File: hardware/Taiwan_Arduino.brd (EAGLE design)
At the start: 97.4 x 35.6 mm, 43 parts, among them J1 AVR_SPI_PRG_62X3_LOCK, T2 2N2222, U1 ATMEGA328P_PDIP, U2 SPI_FLASH, Y2 16mhz

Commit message: add FTDI pin labels
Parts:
- FTDI: value DTR -> (none)
- moved S1 2.04 mm to (18.1, 17.4)
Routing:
- net +5V: track 159.4 -> 144.5 mm
- net RST: track 53.4 -> 47.5 mm
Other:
- board text added: "DTR RXI TXO VCC CTS GND"
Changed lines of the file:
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@@
 <?xml version="1.0" encoding="utf-8"?>
 <!DOCTYPE eagle SYSTEM "eagle.dtd">
-<eagle version="7.4.0">
+<eagle version="7.2.0">
 <drawing>
 <settings>
@@
 <text x="57.3" y="12.1" size="1.016" layer="21" font="vector" ratio="15">22pf</text>
 <text x="47.7" y="37.9" size="1.016" layer="21" font="vector" ratio="15" rot="R180">104</text>
-<text x="21.2" y="20" size="1.016" layer="21" font="vector" ratio="15" rot="R180">Reset</text>
+<text x="25.7" y="21.4" size="1.016" layer="21" font="vector" ratio="15" rot="R180">Reset</text>
 <text x="22.9" y="14.5" size="1.016" layer="21" font="vector" ratio="15">104</text>
 <text x="78.5" y="9.8" size="1.4224" layer="21" font="vector" ratio="15" rot="R180">D6</text>
@@
 <text x="14.7" y="21.4" size="1.4224" layer="21" font="vector" ratio="15">A5</text>
 <text x="66.8" y="8.6" size="1.4224" layer="21" font="vector" ratio="15">D7</text>
+<text x="13.5" y="12" size="0.8128" layer="22" font="vector" ratio="15" distance="60" rot="MR90">DTR
+RXI
+TXO
+VCC
+CTS
+GND</text>
 </plain>
 <attributes>
@@
 <element name="TP8" library="SparkFun-Passives" package="PADBIG" value="TEST-POINT" x="90.575859375" y="17.7033125" rot="R200"/>
 <element name="TP9" library="SparkFun-Passives" package="PADBIG" value="TEST-POINT" x="80.3756375" y="27.159590625" rot="R200"/>
-<element name="FTDI" library="SparkFun-Connectors" package="1X06_LOCK" value="DTR" x="26.8" y="10.4" smashed="yes" rot="R180">
-<attribute name="NAME" x="28.378" y="9.97" size="1.016" layer="25" font="vector" ratio="15" rot="R270"/>
-<attribute name="VALUE" x="27.97" y="9.102" size="1.016" layer="27" font="vector" ratio="15" rot="R180"/>
+<element name="FTDI" library="SparkFun-Connectors" package="1X06_LOCK" value="" x="26.8" y="10.4" smashed="yes" rot="R180">
+<attribute name="NAME" x="26.23" y="7.578" size="1.016" layer="25" font="vector" ratio="15"/>
+<attribute name="VALUE" x="26.77" y="8.902" size="1.016" layer="27" font="vector" ratio="15" rot="R180"/>
 </element>
 <element name="RV1" library="SparkFun-Electromechanical" package="ALPS_POT" value="5k" x="69.229653125" y="20.472284375" smashed="yes" rot="R90">
@@
 <attribute name="NAME" x="50.25269375" y="34.93434375" size="1.016" layer="25" font="vector" ratio="15" rot="R270"/>
 </element>
-<element name="S1" library="SparkFun-Electromechanical" package="TACTILE-PTH" value="SWITCH-MOMENTARY-2PTH" x="17.66" y="15.35" smashed="yes" rot="R180">
-<attribute name="NAME" x="16.016521875" y="20.03429375" size="1.016" layer="25" font="vector" ratio="15" rot="R180"/>
+<element name="S1" library="SparkFun-Electromechanical" package="TACTILE-PTH" value="SWITCH-MOMENTARY-2PTH" x="18.06" y="17.35" smashed="yes" rot="R180">
+<attribute name="NAME" x="14.53429375" y="16.583478125" size="1.016" layer="25" font="vector" ratio="15" rot="R90"/>
 </element>
 <element name="D1" library="SparkFun-LED" package="LED3MM" value="" x="41.3" y="28.6" smashed="yes" rot="R180">
@@
 <wire x1="44.469140625" y1="14.361278125" x2="44.469140625" y2="16.652325" width="0.6096" layer="1"/>
 <wire x1="44.469140625" y1="16.652325" x2="44.048196875" y2="17.17326875" width="0.6096" layer="1"/>
-<wire x1="26" y1="19.44" x2="20.14" y2="19.44" width="0.254" layer="1"/>
-<wire x1="20.14" y1="19.44" x2="19.3" y2="18.6" width="0.254" layer="1"/>
-<wire x1="19.3" y1="18.6" x2="19.3" y2="10.774" width="0.254" layer="1"/>
+<wire x1="26" y1="19.44" x2="21.64" y2="18.44" width="0" layer="19" extent="1-16"/>
+<wire x1="21.64" y1="18.44" x2="19.3" y2="18.6" width="0" layer="19" extent="1-16"/>
+<wire x1="19.3" y1="18.6" x2="19.3" y2="10.774" width="0" layer="19" extent="1-16"/>
 <wire x1="19.3" y1="10.774" x2="19.18" y2="10.654" width="0.254" layer="1"/>
 <wire x1="44.9" y1="36.8" x2="44.2" y2="36" width="1.016" layer="1"/>
@@
 <wire x1="55.2" y1="21.9" x2="56.1" y2="22.8" width="0.254" layer="16"/>
 <via x="56.1" y="22.8" extent="1-16" drill="0.3302"/>
-<wire x1="28.434928125" y1="16.3" x2="28.5" y2="16.2" width="0.254" layer="1"/>
-<wire x1="28.5" y1="16.2" x2="28.6" y2="16.9" width="0.254" layer="1"/>
 <wire x1="28.6" y1="16.9" x2="28.6" y2="20.7" width="0.254" layer="1"/>
 <wire x1="28.6" y1="20.7" x2="29.3" y2="21.4" width="0.254" layer="1"/>
-<wire x1="26" y1="16.9" x2="28.734928125" y2="16.9" width="0.254" layer="1"/>
-<wire x1="28.734928125" y1="16.9" x2="28.808196875" y2="17.17326875" width="0.254" layer="1"/>
 <wire x1="56.1" y1="22.8" x2="57.7" y2="22.8" width="0.254" layer="1"/>
 <wire x1="57.7" y1="22.8" x2="57.9" y2="23" width="0.254" layer="1"/>
 <wire x1="57.9" y1="23" x2="57.9" y2="27.757859375" width="0.254" layer="1"/>
 <wire x1="57.9" y1="27.757859375" x2="57.3817875" y2="28.276071875" width="0.254" layer="1"/>
-<wire x1="26" y1="16.9" x2="22.0218" y2="16.9" width="0.254" layer="1"/>
-<wire x1="22.0218" y1="16.9" x2="20.9112" y2="17.6106" width="0.254" layer="1"/>
 <wire x1="23.2" y1="13.4" x2="23.2" y2="14.1" width="0.254" layer="1"/>
 <wire x1="23.2" y1="14.1" x2="26" y2="16.9" width="0.254" layer="1"/>
-<wire x1="28.734928125" y1="16.9" x2="28.6" y2="16.9" width="0" layer="19" extent="1-1"/>
+<wire x1="28.734928125" y1="16.9" x2="28.808196875" y2="16.97326875" width="0.254" layer="1"/>
+<wire x1="28.808196875" y1="16.97326875" x2="28.808196875" y2="17.17326875" width="0.254" layer="1"/>
+<wire x1="26" y1="16.9" x2="28.534928125" y2="16.9" width="0.254" layer="1"/>
+<wire x1="28.534928125" y1="16.9" x2="28.808196875" y2="17.17326875" width="0.254" layer="1"/>
+<wire x1="28.534928125" y1="16.9" x2="28.6" y2="16.9" width="0" layer="19" extent="1-1"/>
+<wire x1="21.3112" y1="19.6106" x2="23.2" y2="13.4" width="0" layer="19" extent="1-1"/>
 </signal>
 <signal name="N$10">

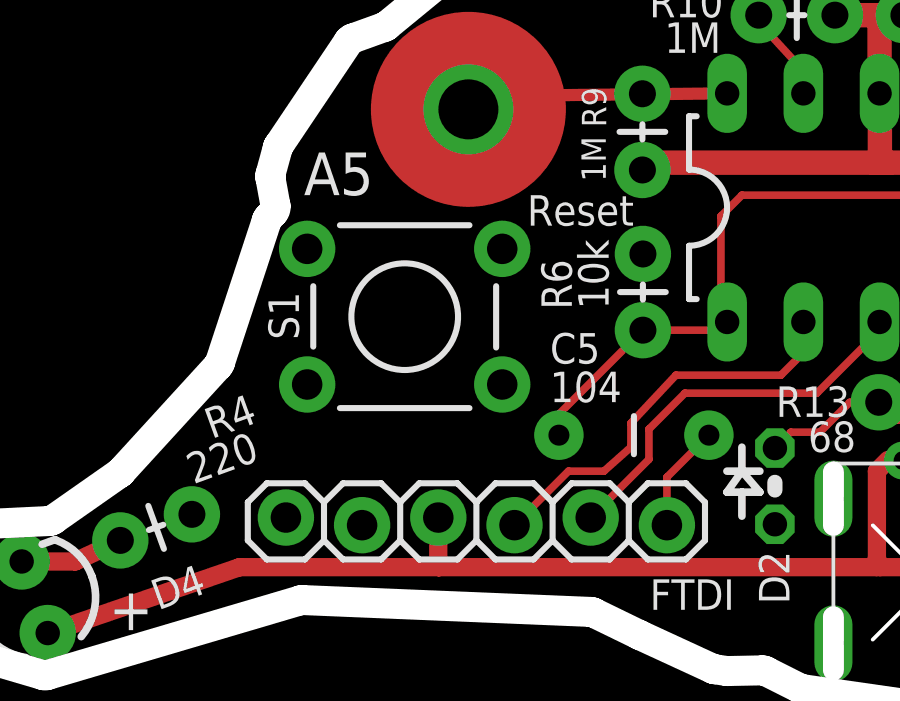
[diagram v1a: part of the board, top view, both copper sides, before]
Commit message: add FTDI Tag
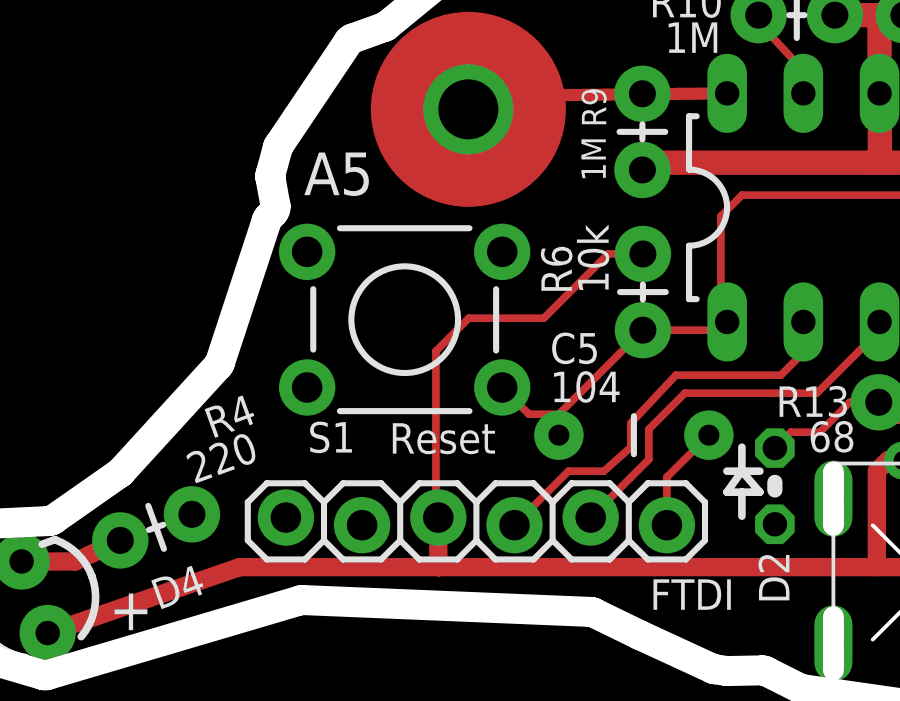
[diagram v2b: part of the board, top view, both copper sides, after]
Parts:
- moved S1 0.10 mm to (18.1, 17.2)
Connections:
- net GND: now also S1.3; no longer S1.1
- net RST: now also S1.1; no longer S1.3
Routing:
- net +5V: track 144.5 -> 158.4 mm
- net RST: track 47.5 -> 49.7 mm
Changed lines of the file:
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@@
 <?xml version="1.0" encoding="utf-8"?>
 <!DOCTYPE eagle SYSTEM "eagle.dtd">
-<eagle version="7.2.0">
+<eagle version="7.4.0">
 <drawing>
 <settings>
@@
 <text x="57.3" y="12.1" size="1.016" layer="21" font="vector" ratio="15">22pf</text>
 <text x="47.7" y="37.9" size="1.016" layer="21" font="vector" ratio="15" rot="R180">104</text>
-<text x="25.7" y="21.4" size="1.016" layer="21" font="vector" ratio="15" rot="R180">Reset</text>
+<text x="21.1" y="13.8" size="1.016" layer="21" font="vector" ratio="15" rot="R180">Reset</text>
 <text x="22.9" y="14.5" size="1.016" layer="21" font="vector" ratio="15">104</text>
 <text x="78.5" y="9.8" size="1.4224" layer="21" font="vector" ratio="15" rot="R180">D6</text>
@@
 </element>
 <element name="R6" library="SparkFun-Resistors" package="AXIAL-0.1" value="10k" x="26" y="16.9" smashed="yes" rot="R90">
-<attribute name="NAME" x="23.632265625" y="17.5885625" size="1.016" layer="25" font="vector" ratio="15" rot="R90"/>
-<attribute name="VALUE" x="24.859" y="17.6" size="1.016" layer="21" font="vector" ratio="15" rot="R90"/>
+<attribute name="NAME" x="23.632265625" y="18.0885625" size="1.016" layer="25" font="vector" ratio="15" rot="R90"/>
+<attribute name="VALUE" x="24.859" y="18.1" size="1.016" layer="21" font="vector" ratio="15" rot="R90"/>
 </element>
 <element name="U1" library="SparkFun-DigitalIC" package="DIL28-3" value="ATMEGA328P_PDIP" x="45.318196875" y="20.98326875" smashed="yes">
@@
 <attribute name="NAME" x="50.25269375" y="34.93434375" size="1.016" layer="25" font="vector" ratio="15" rot="R270"/>
 </element>
-<element name="S1" library="SparkFun-Electromechanical" package="TACTILE-PTH" value="SWITCH-MOMENTARY-2PTH" x="18.06" y="17.35" smashed="yes" rot="R180">
-<attribute name="NAME" x="14.53429375" y="16.583478125" size="1.016" layer="25" font="vector" ratio="15" rot="R90"/>
+<element name="S1" library="SparkFun-Electromechanical" package="TACTILE-PTH" value="SWITCH-MOMENTARY-2PTH" x="18.06" y="17.25" smashed="yes" rot="R180">
+<attribute name="NAME" x="16.416521875" y="13.83429375" size="1.016" layer="25" font="vector" ratio="15" rot="R180"/>
 </element>
 <element name="D1" library="SparkFun-LED" package="LED3MM" value="" x="41.3" y="28.6" smashed="yes" rot="R180">
@@
 <contactref element="C1" pad="-"/>
 <contactref element="R3" pad="P$2"/>
-<contactref element="S1" pad="1"/>
 <contactref element="C2" pad="2"/>
 <contactref element="C2" pad="2"/>
@@
 <contactref element="RV1" pad="P$1"/>
 <contactref element="JP1" pad="1"/>
+<contactref element="S1" pad="3"/>
 </signal>
 <signal name="+5V">
@@
 <wire x1="44.469140625" y1="14.361278125" x2="44.469140625" y2="16.652325" width="0.6096" layer="1"/>
 <wire x1="44.469140625" y1="16.652325" x2="44.048196875" y2="17.17326875" width="0.6096" layer="1"/>
-<wire x1="26" y1="19.44" x2="21.64" y2="18.44" width="0" layer="19" extent="1-16"/>
-<wire x1="21.64" y1="18.44" x2="19.3" y2="18.6" width="0" layer="19" extent="1-16"/>
-<wire x1="19.3" y1="18.6" x2="19.3" y2="10.774" width="0" layer="19" extent="1-16"/>
 <wire x1="19.3" y1="10.774" x2="19.18" y2="10.654" width="0.254" layer="1"/>
 <wire x1="44.9" y1="36.8" x2="44.2" y2="36" width="1.016" layer="1"/>
@@
 <wire x1="46.4" y1="30.7" x2="46.4" y2="30.33335" width="1.016" layer="1"/>
 <wire x1="46.4" y1="30.33335" x2="46.66565625" y2="30.06769375" width="1.016" layer="1"/>
+<wire x1="26" y1="19.44" x2="24.84" y2="19.44" width="0.254" layer="1"/>
+<wire x1="24.84" y1="19.44" x2="22.7" y2="17.3" width="0.254" layer="1"/>
+<wire x1="22.7" y1="17.3" x2="20.2" y2="17.3" width="0.254" layer="1"/>
+<wire x1="20.2" y1="17.3" x2="19.1" y2="16.2" width="0.254" layer="1"/>
+<wire x1="19.1" y1="16.2" x2="19.1" y2="10.734" width="0.254" layer="1"/>
+<wire x1="19.1" y1="10.734" x2="19.18" y2="10.654" width="0.254" layer="1"/>
 </signal>
 <signal name="N$15">
@@
 <contactref element="R6" pad="P$1"/>
 <contactref element="C5" pad="1"/>
-<contactref element="S1" pad="3"/>
 <wire x1="29.3" y1="21.4" x2="51.6" y2="21.4" width="0.254" layer="1"/>
 <wire x1="51.6" y1="21.4" x2="51.6" y2="21.5" width="0.254" layer="1"/>
@@
 <wire x1="26" y1="16.9" x2="28.534928125" y2="16.9" width="0.254" layer="1"/>
 <wire x1="28.534928125" y1="16.9" x2="28.808196875" y2="17.17326875" width="0.254" layer="1"/>
+<contactref element="S1" pad="1"/>
+<wire x1="23.2" y1="14.1" x2="22.2006" y2="14.1" width="0.254" layer="1"/>
+<wire x1="22.2006" y1="14.1" x2="21.3112" y2="14.9894" width="0.254" layer="1"/>
 <wire x1="28.534928125" y1="16.9" x2="28.6" y2="16.9" width="0" layer="19" extent="1-1"/>
-<wire x1="21.3112" y1="19.6106" x2="23.2" y2="13.4" width="0" layer="19" extent="1-1"/>
 </signal>
 <signal name="N$10">

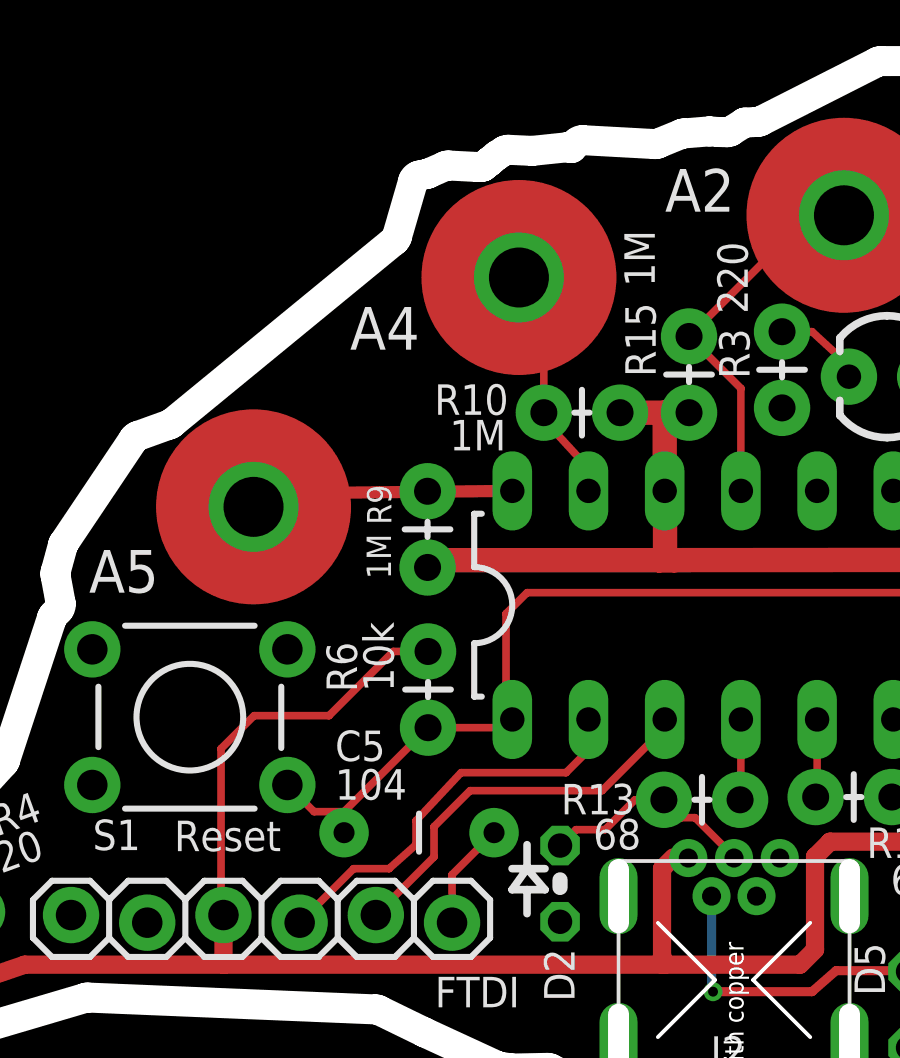
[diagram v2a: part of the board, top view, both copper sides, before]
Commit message: add FTDI Tag
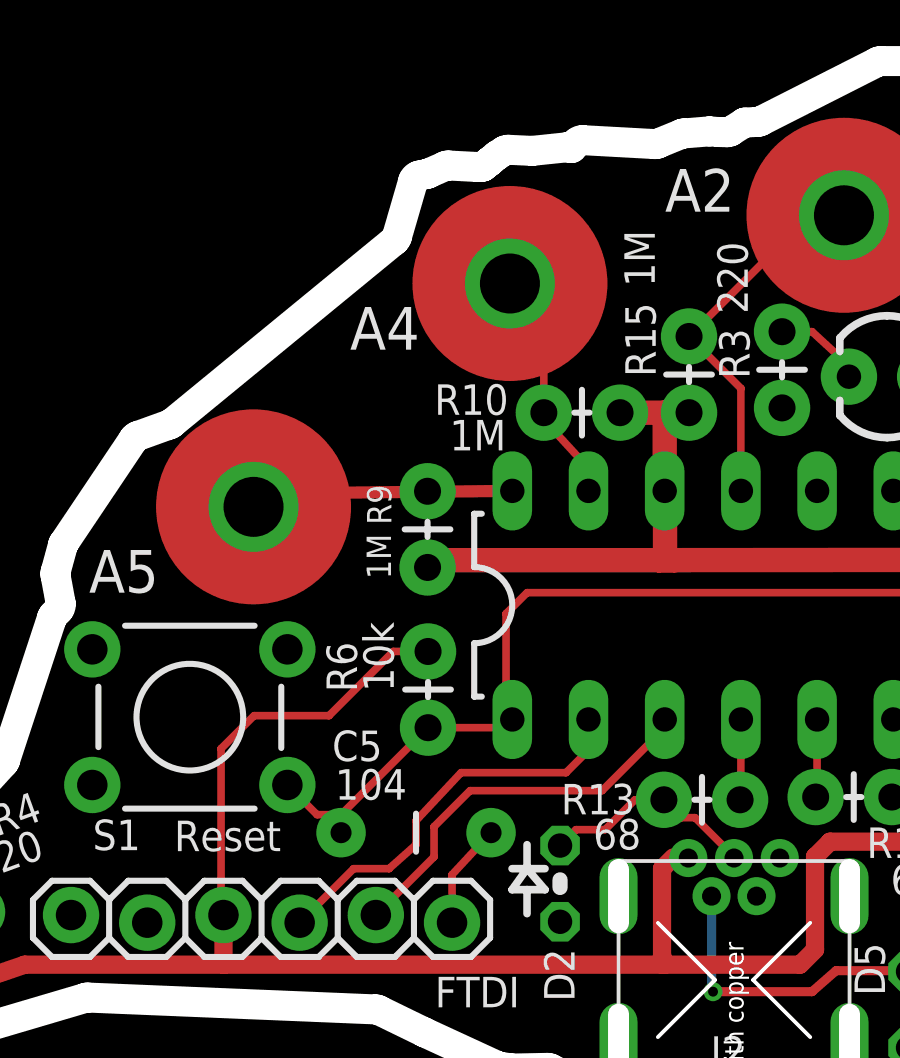
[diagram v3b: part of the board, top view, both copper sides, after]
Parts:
- moved TP2 0.36 mm to (28.7, 31.7)
- moved C5 0.10 mm to (25.6, 13.4)
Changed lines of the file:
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@@
 <element name="TP3" library="SparkFun-Passives" package="PADBIG" value="TEST-POINT" x="81.94820625" y="11.284709375" rot="R290"/>
 <element name="TP1" library="SparkFun-Passives" package="PADBIG" value="TEST-POINT" x="39.863778125" y="33.9791" rot="R290"/>
-<element name="TP2" library="SparkFun-Passives" package="PADBIG" value="TEST-POINT" x="29.029615625" y="31.90571875" rot="R290"/>
+<element name="TP2" library="SparkFun-Passives" package="PADBIG" value="TEST-POINT" x="28.729615625" y="31.70571875" rot="R290"/>
 <element name="TP4" library="SparkFun-Passives" package="PADBIG" value="TEST-POINT" x="20.183053125" y="24.260109375" rot="R290"/>
 <element name="TP6" library="SparkFun-Passives" package="PADBIG" value="TEST-POINT" x="63.69446875" y="10.9264875" rot="R290"/>
@@
 <attribute name="VALUE" x="11.01875625" y="11.76299375" size="1.016" layer="21" font="vector" ratio="15" rot="R20"/>
 </element>
-<element name="C5" library="SparkFun-Capacitors" package="CAP-PTH-5MM" value="0.1uF" x="25.7" y="13.4" smashed="yes">
-<attribute name="NAME" x="22.90335625" y="15.786609375" size="1.016" layer="25" font="vector" ratio="15"/>
+<element name="C5" library="SparkFun-Capacitors" package="CAP-PTH-5MM" value="0.1uF" x="25.6" y="13.4" smashed="yes">
+<attribute name="NAME" x="22.80335625" y="15.786609375" size="1.016" layer="25" font="vector" ratio="15"/>
 </element>
 <element name="JP3" library="SparkFun-Connectors" package="1X02_NO_SILK" value="M021X02_NO_SILK" x="86.01123125" y="19.4878375" smashed="yes" rot="R90">
@@
 <wire x1="57.9" y1="23" x2="57.9" y2="27.757859375" width="0.254" layer="1"/>
 <wire x1="57.9" y1="27.757859375" x2="57.3817875" y2="28.276071875" width="0.254" layer="1"/>
-<wire x1="23.2" y1="13.4" x2="23.2" y2="14.1" width="0.254" layer="1"/>
-<wire x1="23.2" y1="14.1" x2="26" y2="16.9" width="0.254" layer="1"/>
+<wire x1="23.1" y1="13.4" x2="23.1" y2="14" width="0.254" layer="1"/>
+<wire x1="23.1" y1="14" x2="26" y2="16.9" width="0.254" layer="1"/>
 <wire x1="28.734928125" y1="16.9" x2="28.808196875" y2="16.97326875" width="0.254" layer="1"/>
 <wire x1="28.808196875" y1="16.97326875" x2="28.808196875" y2="17.17326875" width="0.254" layer="1"/>
@@
 <wire x1="28.534928125" y1="16.9" x2="28.808196875" y2="17.17326875" width="0.254" layer="1"/>
 <contactref element="S1" pad="1"/>
-<wire x1="23.2" y1="14.1" x2="22.2006" y2="14.1" width="0.254" layer="1"/>
-<wire x1="22.2006" y1="14.1" x2="21.3112" y2="14.9894" width="0.254" layer="1"/>
+<wire x1="23.1" y1="14" x2="22.3006" y2="14" width="0.254" layer="1"/>
+<wire x1="22.3006" y1="14" x2="21.3112" y2="14.9894" width="0.254" layer="1"/>
 <wire x1="28.534928125" y1="16.9" x2="28.6" y2="16.9" width="0" layer="19" extent="1-1"/>
 </signal>
@@
 <wire x1="29.86" y1="29.94" x2="29.8" y2="30.2" width="0.254" layer="1"/>
 <wire x1="29.8" y1="30.2" x2="29.86" y2="31.175334375" width="0.254" layer="1"/>
-<wire x1="29.86" y1="31.175334375" x2="29.029615625" y2="31.90571875" width="0.254" layer="1"/>
+<wire x1="29.86" y1="31.175334375" x2="28.729615625" y2="31.70571875" width="0.254" layer="1"/>
 </signal>
 <signal name="N$8">
@@
 <contactref element="C5" pad="2"/>
 <wire x1="26.8" y1="10.4" x2="26.8" y2="12" width="0.254" layer="1"/>
-<wire x1="26.8" y1="12" x2="28.2" y2="13.4" width="0.254" layer="1"/>
+<wire x1="26.8" y1="12" x2="28.1" y2="13.4" width="0.254" layer="1"/>
 </signal>
 <signal name="N$28">
